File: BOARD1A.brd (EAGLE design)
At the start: 100 x 80 mm, 37 parts, among them U1 MCP23008

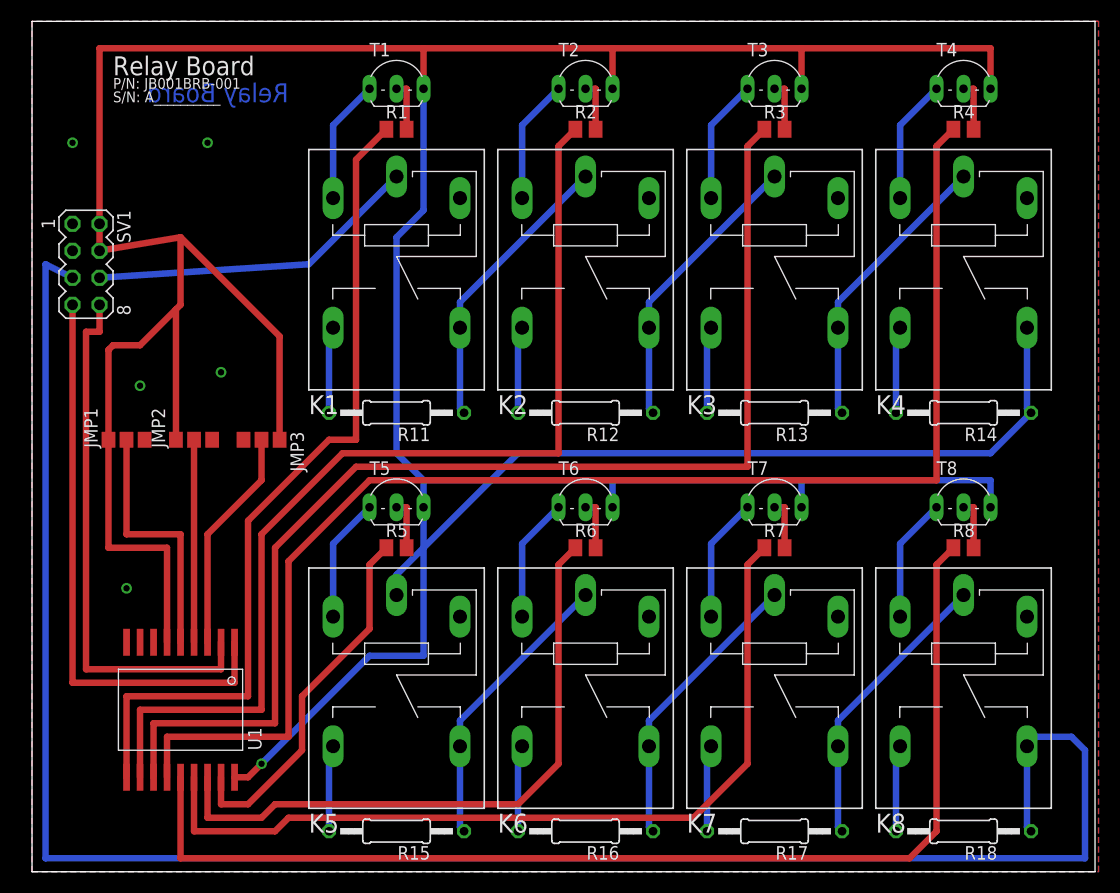
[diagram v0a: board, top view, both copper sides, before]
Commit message: Added Silk Screens, Changed Layout some.
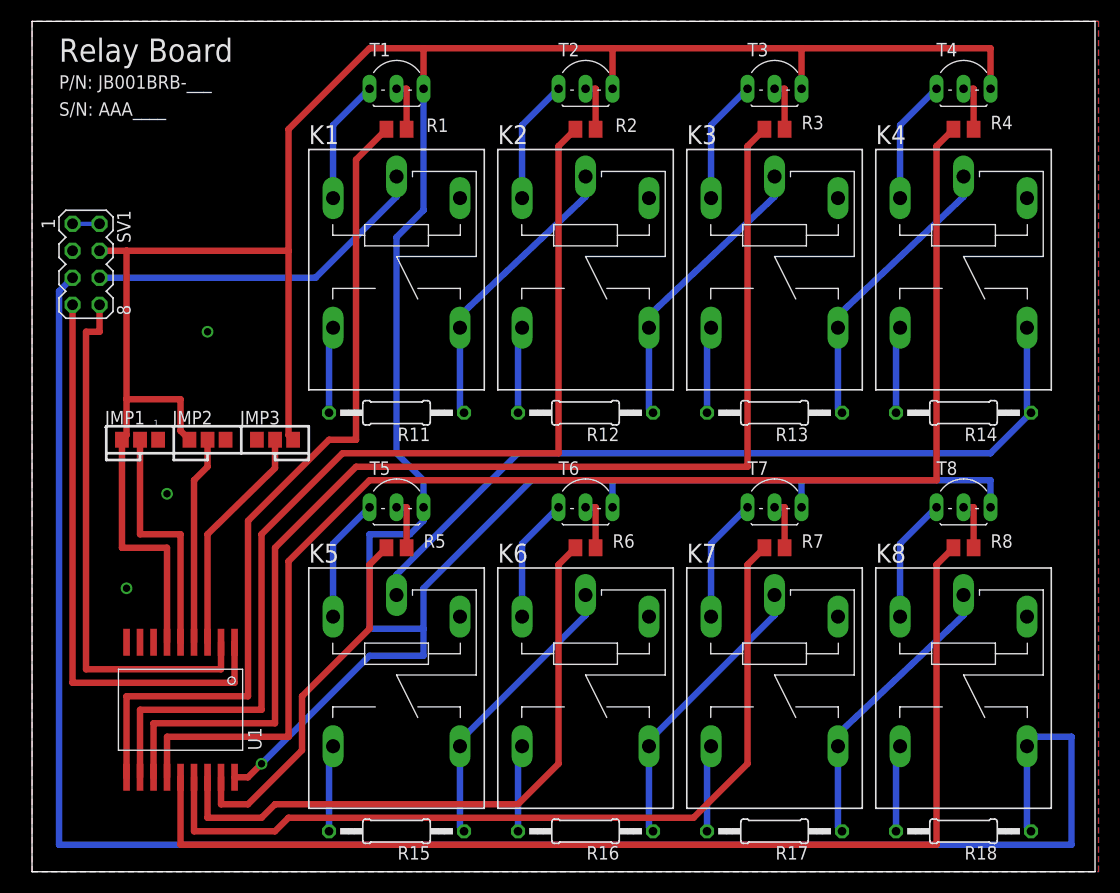
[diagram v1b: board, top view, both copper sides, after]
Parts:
- moved JMP2 1.27 mm to (16.5, 40.6)
- moved JMP1 1.27 mm to (10.2, 40.6)
- moved JMP3 1.27 mm to (22.9, 40.6)
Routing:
- net +5V: track 347.8 -> 338.4 mm
- net OUTPUT: track 181.2 -> 172.0 mm
- net N$5: track 0.00 -> 2.54 mm
- net INPUT: track 31.4 -> 33.0 mm
- net A0ADDR: track 24.1 -> 22.9 mm
- net K8: track 107.1 -> 106.1 mm
- net A2ADDR: track 21.2 -> 21.7 mm
- net A1ADDR: track 19.1 -> 19.6 mm
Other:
- board text added: "1"
- board text added: "P/N: JB001BRB-___"
- board text added: "S/N: AAA____"
- board text removed: "P/N: JB001BRB-001"
- board text removed: "S/N: A__________"

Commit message: Changed Parts
Changed relay from 5VDC Coil to 12 VDC so it’s only 40mA. Changed to
SOT-23 SBT Transistor (100mA capability). removed bias resistors.
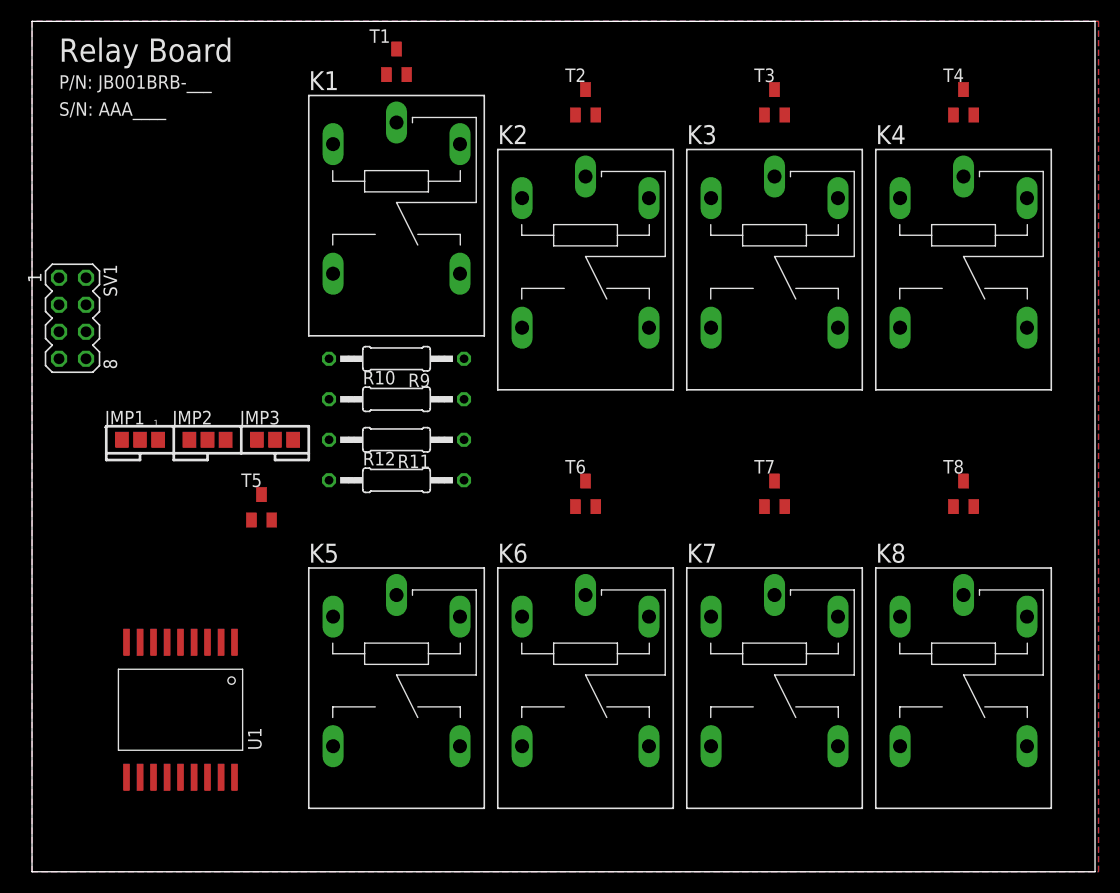
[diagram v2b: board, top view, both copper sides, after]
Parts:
- removed R1, R2, R3, R4, R5, R6, R7, R8: (no value), resistor:M0805
- removed R13, R14, R15, R16, R17, R18: (no value), resistor:0207/12
- added R10, R9: (no value), resistor:0207/12
- K1: value (none) -> G5LE-1-VD DC12
- T1, T2, T3, T4, T5, T6, T7, T8: device transistor:TO92-EBC -> transistor-neu-to92:SC59-BEC
- moved R12 18.9 mm to (34.3, 36.8), turned to 0 degrees
- moved T5 12.8 mm to (21.6, 34.3)
- moved SV1 5.24 mm to (3.81, 52.1)
- moved K1 5.08 mm to (34.3, 61.0)
- moved T2 2.54 mm to (52.1, 72.4)
- moved T3 2.54 mm to (69.8, 72.4)
- moved T4 2.54 mm to (87.6, 72.4)
- moved R11 2.54 mm to (34.3, 40.6)
- moved T1 1.27 mm to (34.3, 76.2)
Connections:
- removed net N$110: K1.NO, R11.2
- removed net N$111: K1.NC, K2.COM, R11.1
- removed net N$112: K2.NO, R12.2
- removed net N$113: K2.NC, K3.COM, R12.1
- removed net N$114: K3.NC, K4.COM, R13.1
- removed net N$115: K3.NO, R13.2
- removed net N$116: K4.NC, K5.COM, R14.1
- removed net N$117: K4.NO, R14.2
- removed net N$118: K5.NC, K6.COM, R15.1
- removed net N$119: K5.NO, R15.2
- net K1: no longer R1.1
- net K2: no longer R2.1
- net K3: no longer R3.1
- net K4: no longer R4.1
- net K5: no longer R5.1
- net K6: no longer R6.1
- net K7: no longer R7.1
- net K8: no longer R8.1
- net N$1: now also K1.NO, R9.2; no longer K6.NO, R16.2
- net N$12: no longer R1.2
- net N$14: no longer R2.2
- net N$16: no longer R3.2
- net N$18: no longer R4.2
- net N$2: now also R10.2, R9.1; no longer K6.NC, K7.COM, R16.1
- net N$20: no longer R5.2
- net N$22: no longer R6.2
- net N$24: no longer R7.2
- net N$26: no longer R8.2
- net N$3: now also R10.1, R11.2; no longer K7.NO, R17.2
- net N$4: now also R11.1, R12.2; no longer K7.NC, K8.COM, R17.1
- net N$6: now also K1.NC, R12.1; no longer K8.NO, R18.2
- net OUTPUT: no longer K8.NC, R18.1
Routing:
- net +5V: track 338.4 -> 0.00 mm, vias 1 -> 0
- net OUTPUT: track 172.0 -> 0.00 mm
- net K4: track 129.5 -> 0.00 mm
- net K3: track 113.0 -> 0.00 mm
- net K8: track 106.1 -> 0.00 mm
- net K2: track 96.5 -> 0.00 mm
- net K7: track 80.8 -> 0.00 mm
- net K1: track 79.3 -> 0.00 mm
- net N$116: track 76.1 -> 0.00 mm
- net K6: track 59.9 -> 0.00 mm
- net SCL: track 54.6 -> 0.00 mm
- net SDA: track 50.8 -> 0.00 mm
- net K5: track 34.6 -> 0.00 mm
- net INPUT: track 33.0 -> 0.00 mm
- net N$111: track 27.5 -> 0.00 mm
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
